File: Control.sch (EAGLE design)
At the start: 20 parts, among them IC1 MEGA8-P, Q1 16MHz, T1 2N2222, X1 MKDSN1,5/3-5,08, X2 MKDSN1,5/3-5,08

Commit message: updated schematic and board
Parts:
- added R7: 120K, rcl:R-US_0207/7
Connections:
- net GND: now also R7.2
- net N$18: now also R7.1
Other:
- moved on the sheet: PROG-HDR
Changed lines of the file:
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@@
 <part name="P+5" library="supply1" deviceset="+5V" device=""/>
 <part name="GND6" library="supply1" deviceset="GND" device=""/>
+<part name="R7" library="rcl" deviceset="R-US_" device="0207/7" value="120K"/>
+<part name="GND10" library="supply1" deviceset="GND" device=""/>
 </parts>
 <sheets>
@@
 <instance part="C2" gate="G$1" x="43.18" y="71.12"/>
 <instance part="IC1" gate="G$1" x="124.46" y="73.66"/>
-<instance part="PROG-HDR" gate="1" x="182.88" y="43.18"/>
+<instance part="PROG-HDR" gate="1" x="175.26" y="43.18"/>
 <instance part="P+1" gate="1" x="58.42" y="81.28"/>
 <instance part="P+2" gate="1" x="96.52" y="111.76"/>
@@
 <instance part="P+5" gate="1" x="86.36" y="66.04"/>
 <instance part="GND6" gate="1" x="86.36" y="53.34"/>
+<instance part="R7" gate="G$1" x="170.18" y="88.9" smashed="yes">
+<attribute name="NAME" x="166.37" y="90.3986" size="1.778" layer="95"/>
+<attribute name="VALUE" x="171.45" y="90.678" size="1.778" layer="96"/>
+</instance>
+<instance part="GND10" gate="1" x="175.26" y="86.36"/>
 </instances>
 <busses>
@@
 <pinref part="PROG-HDR" gate="1" pin="1"/>
 <pinref part="GND5" gate="1" pin="GND"/>
+<wire x1="182.88" y1="40.64" x2="190.5" y2="40.64" width="0.1524" layer="91"/>
 <wire x1="190.5" y1="40.64" x2="190.5" y2="38.1" width="0.1524" layer="91"/>
 </segment>
@@
 <pinref part="GND6" gate="1" pin="GND"/>
 </segment>
+<segment>
+<pinref part="R7" gate="G$1" pin="2"/>
+<pinref part="GND10" gate="1" pin="GND"/>
+</segment>
 </net>
 <net name="N$4" class="0">
@@
 <segment>
 <pinref part="IC1" gate="G$1" pin="PB4(MISO)"/>
-<wire x1="149.86" y1="45.72" x2="175.26" y2="45.72" width="0.1524" layer="91"/>
+<wire x1="149.86" y1="45.72" x2="167.64" y2="45.72" width="0.1524" layer="91"/>
 <pinref part="PROG-HDR" gate="1" pin="6"/>
 </segment>
@@
 <segment>
 <pinref part="IC1" gate="G$1" pin="PB5(SCK)"/>
-<wire x1="149.86" y1="43.18" x2="175.26" y2="43.18" width="0.1524" layer="91"/>
+<wire x1="149.86" y1="43.18" x2="167.64" y2="43.18" width="0.1524" layer="91"/>
 <pinref part="PROG-HDR" gate="1" pin="4"/>
 </segment>
@@
 <segment>
 <pinref part="PROG-HDR" gate="1" pin="2"/>
-<wire x1="175.26" y1="40.64" x2="175.26" y2="35.56" width="0.1524" layer="91"/>
-<wire x1="175.26" y1="35.56" x2="93.98" y2="35.56" width="0.1524" layer="91"/>
+<wire x1="167.64" y1="40.64" x2="167.64" y2="35.56" width="0.1524" layer="91"/>
+<wire x1="167.64" y1="35.56" x2="93.98" y2="35.56" width="0.1524" layer="91"/>
 <wire x1="93.98" y1="35.56" x2="93.98" y2="101.6" width="0.1524" layer="91"/>
 <pinref part="IC1" gate="G$1" pin="PC6(/RESET)"/>
@@
 <pinref part="PROG-HDR" gate="1" pin="5"/>
 <pinref part="P+3" gate="1" pin="+5V"/>
+<wire x1="182.88" y1="45.72" x2="190.5" y2="45.72" width="0.1524" layer="91"/>
 <wire x1="190.5" y1="45.72" x2="190.5" y2="50.8" width="0.1524" layer="91"/>
 </segment>
@@
 <wire x1="167.64" y1="55.88" x2="193.04" y2="55.88" width="0.1524" layer="91"/>
 <wire x1="193.04" y1="55.88" x2="193.04" y2="43.18" width="0.1524" layer="91"/>
-<wire x1="193.04" y1="43.18" x2="190.5" y2="43.18" width="0.1524" layer="91"/>
+<wire x1="193.04" y1="43.18" x2="182.88" y2="43.18" width="0.1524" layer="91"/>
 </segment>
 </net>
@@
 <pinref part="R1" gate="G$1" pin="1"/>
 <wire x1="149.86" y1="55.88" x2="165.1" y2="55.88" width="0.1524" layer="91"/>
-<wire x1="165.1" y1="55.88" x2="165.1" y2="96.52" width="0.1524" layer="91"/>
-</segment>
-</net>
+<wire x1="165.1" y1="55.88" x2="165.1" y2="88.9" width="0.1524" layer="91"/>
+<pinref part="R7" gate="G$1" pin="1"/>
+<wire x1="165.1" y1="88.9" x2="165.1" y2="96.52" width="0.1524" layer="91"/>
+<junction x="165.1" y="88.9"/>
+</segment>
+</net>

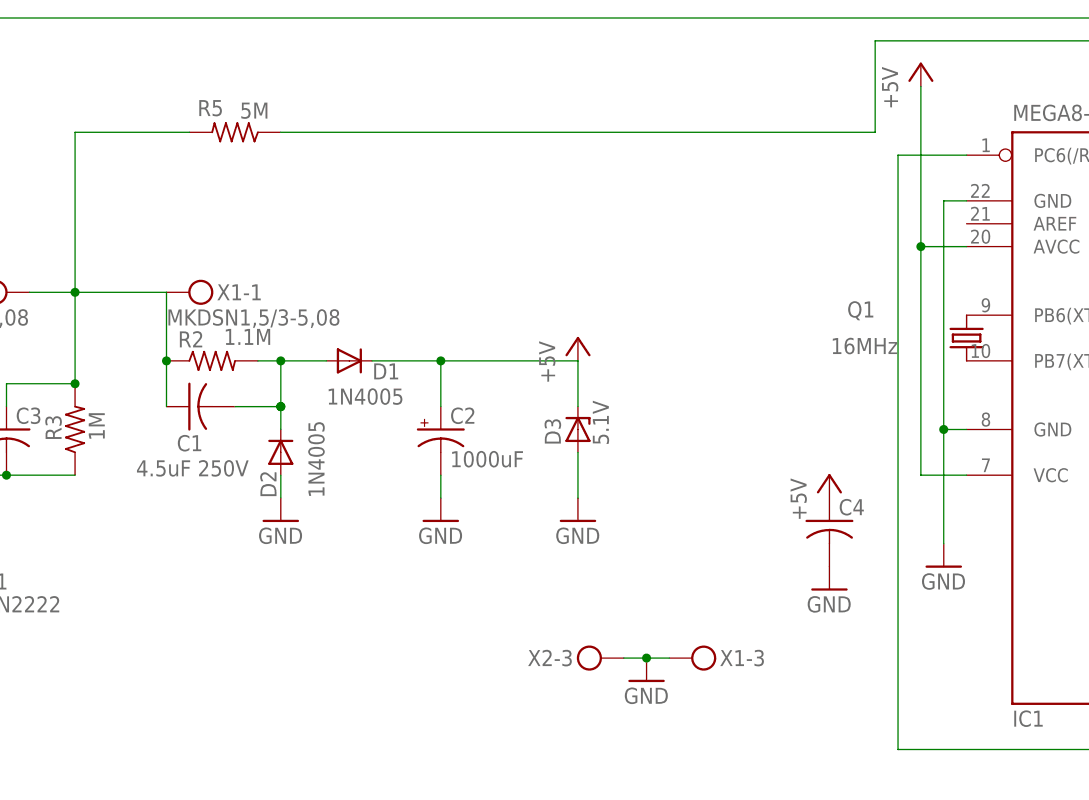
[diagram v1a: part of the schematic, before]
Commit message: Updated schematic and board to add needed pullup resistor to reset pin on Atmega. Also added surface mount pads for local filter capacitor. Pullup resistor located to fit inside central channel of a DIP socket. Changes needed discovered at first hardware assembly.
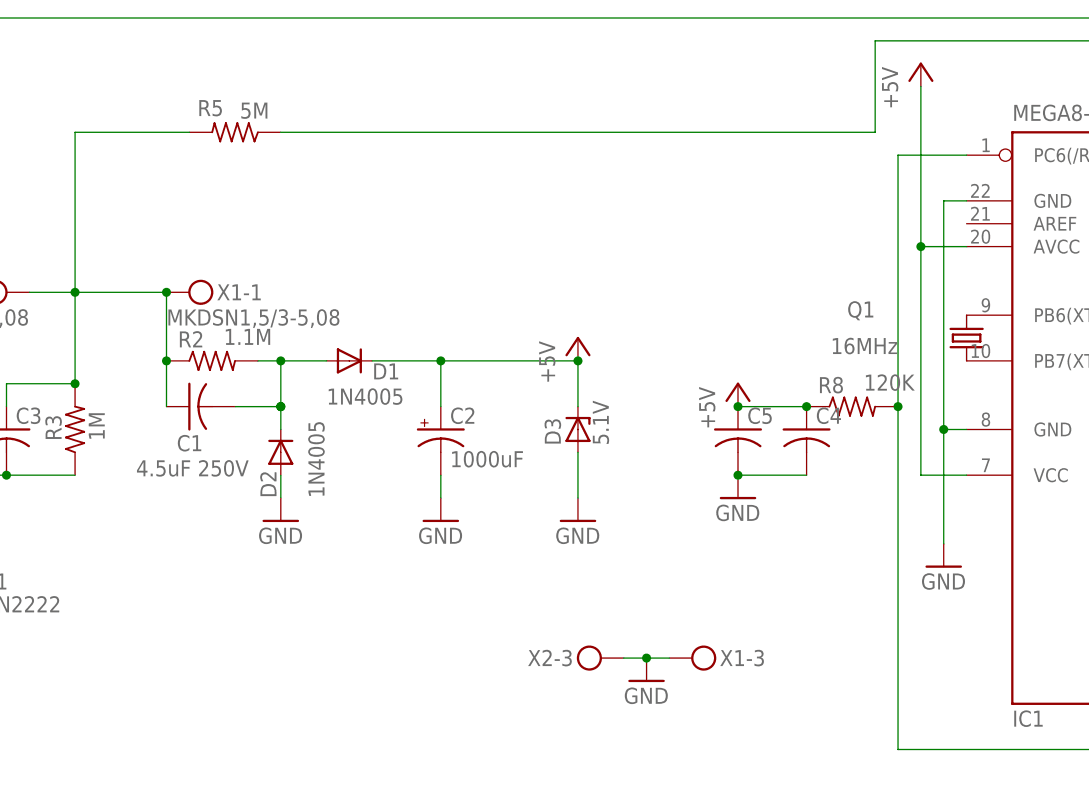
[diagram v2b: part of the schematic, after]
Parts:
- added C5: (no value), rcl:C-USC0402K
- added R8: 120K, rcl:R-US_0207/7
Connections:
- net +5V: now also C5.1, R8.1
- net GND: now also C5.2
- net N$8: now also R8.2
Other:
- moved on the sheet: C4
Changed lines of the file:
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@@
 <part name="R7" library="rcl" deviceset="R-US_" device="0207/7" value="120K"/>
 <part name="GND10" library="supply1" deviceset="GND" device=""/>
+<part name="R8" library="rcl" deviceset="R-US_" device="0207/7" value="120K"/>
+<part name="C5" library="rcl" deviceset="C-US" device="C0402K"/>
 </parts>
 <sheets>
@@
 <attribute name="VALUE" x="93.98" y="81.28" size="1.778" layer="96" rot="R180"/>
 </instance>
-<instance part="C4" gate="G$1" x="86.36" y="60.96"/>
-<instance part="P+5" gate="1" x="86.36" y="66.04"/>
-<instance part="GND6" gate="1" x="86.36" y="53.34"/>
+<instance part="C4" gate="G$1" x="83.82" y="71.12"/>
+<instance part="P+5" gate="1" x="76.2" y="76.2"/>
+<instance part="GND6" gate="1" x="76.2" y="63.5"/>
 <instance part="R7" gate="G$1" x="170.18" y="88.9" smashed="yes">
 <attribute name="NAME" x="166.37" y="90.3986" size="1.778" layer="95"/>
@@
 </instance>
 <instance part="GND10" gate="1" x="175.26" y="86.36"/>
+<instance part="R8" gate="G$1" x="88.9" y="73.66" smashed="yes">
+<attribute name="NAME" x="85.09" y="75.1586" size="1.778" layer="95"/>
+<attribute name="VALUE" x="90.17" y="75.438" size="1.778" layer="96"/>
+</instance>
+<instance part="C5" gate="G$1" x="76.2" y="71.12"/>
 </instances>
 <busses>
@@
 <pinref part="C4" gate="G$1" pin="2"/>
 <pinref part="GND6" gate="1" pin="GND"/>
+<wire x1="76.2" y1="66.04" x2="83.82" y2="66.04" width="0.1524" layer="91"/>
+<pinref part="C5" gate="G$1" pin="2"/>
+<junction x="76.2" y="66.04"/>
 </segment>
 <segment>
@@
 <wire x1="167.64" y1="40.64" x2="167.64" y2="35.56" width="0.1524" layer="91"/>
 <wire x1="167.64" y1="35.56" x2="93.98" y2="35.56" width="0.1524" layer="91"/>
-<wire x1="93.98" y1="35.56" x2="93.98" y2="101.6" width="0.1524" layer="91"/>
+<wire x1="93.98" y1="35.56" x2="93.98" y2="73.66" width="0.1524" layer="91"/>
 <pinref part="IC1" gate="G$1" pin="PC6(/RESET)"/>
+<wire x1="93.98" y1="73.66" x2="93.98" y2="101.6" width="0.1524" layer="91"/>
 <wire x1="93.98" y1="101.6" x2="101.6" y2="101.6" width="0.1524" layer="91"/>
+<pinref part="R8" gate="G$1" pin="2"/>
+<junction x="93.98" y="73.66"/>
 </segment>
 </net>
@@
 <wire x1="58.42" y1="78.74" x2="43.18" y2="78.74" width="0.1524" layer="91"/>
 <junction x="43.18" y="78.74"/>
+<junction x="58.42" y="78.74"/>
 </segment>
 <segment>
@@
 <pinref part="C4" gate="G$1" pin="1"/>
 <pinref part="P+5" gate="1" pin="+5V"/>
+<pinref part="R8" gate="G$1" pin="1"/>
+<wire x1="76.2" y1="73.66" x2="83.82" y2="73.66" width="0.1524" layer="91"/>
+<junction x="83.82" y="73.66"/>
+<pinref part="C5" gate="G$1" pin="1"/>
+<junction x="76.2" y="73.66"/>
 </segment>
 </net>
@@
 <junction x="2.54" y="86.36"/>
 <junction x="2.54" y="76.2"/>
+<junction x="12.7" y="86.36"/>
 </segment>
 </net>
@@
 </sheet>
 </sheets>
+<errors>
+</errors>
 </schematic>
 </drawing>

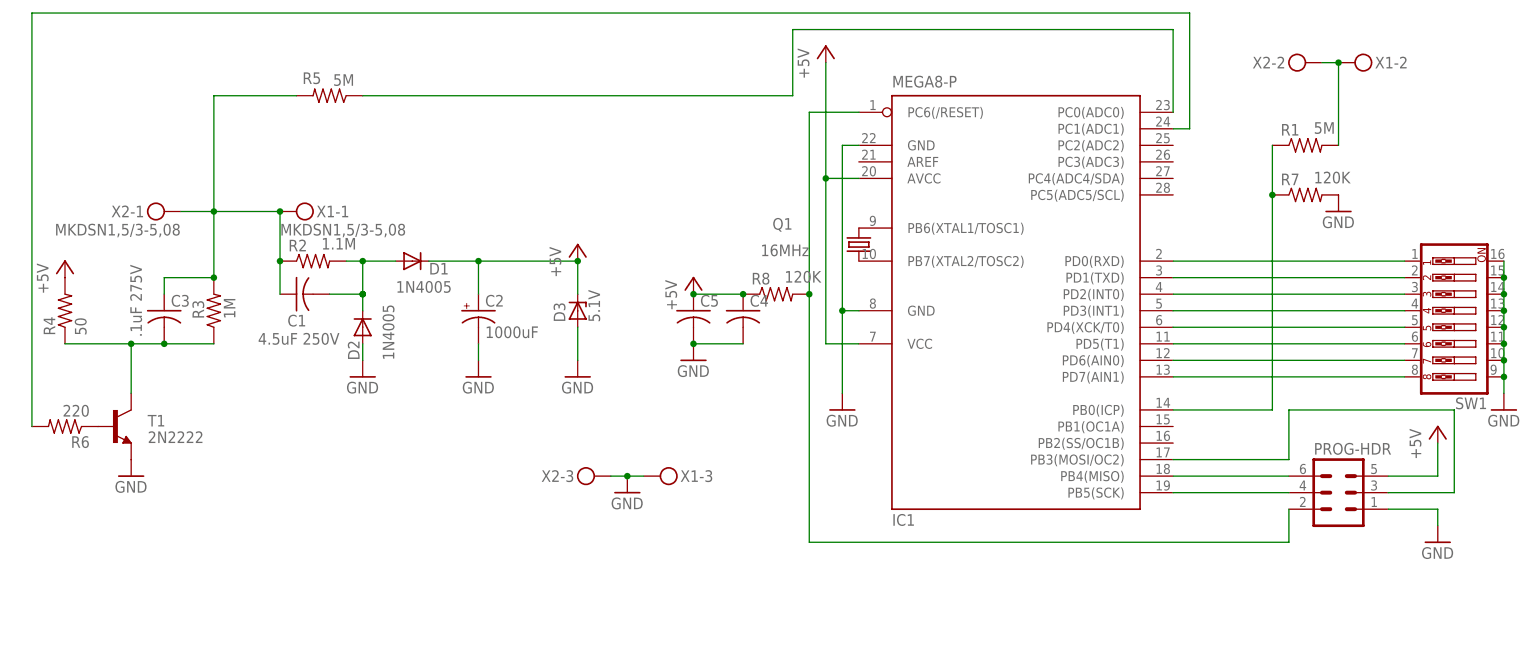
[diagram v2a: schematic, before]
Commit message: Added surface mount options for low voltage section
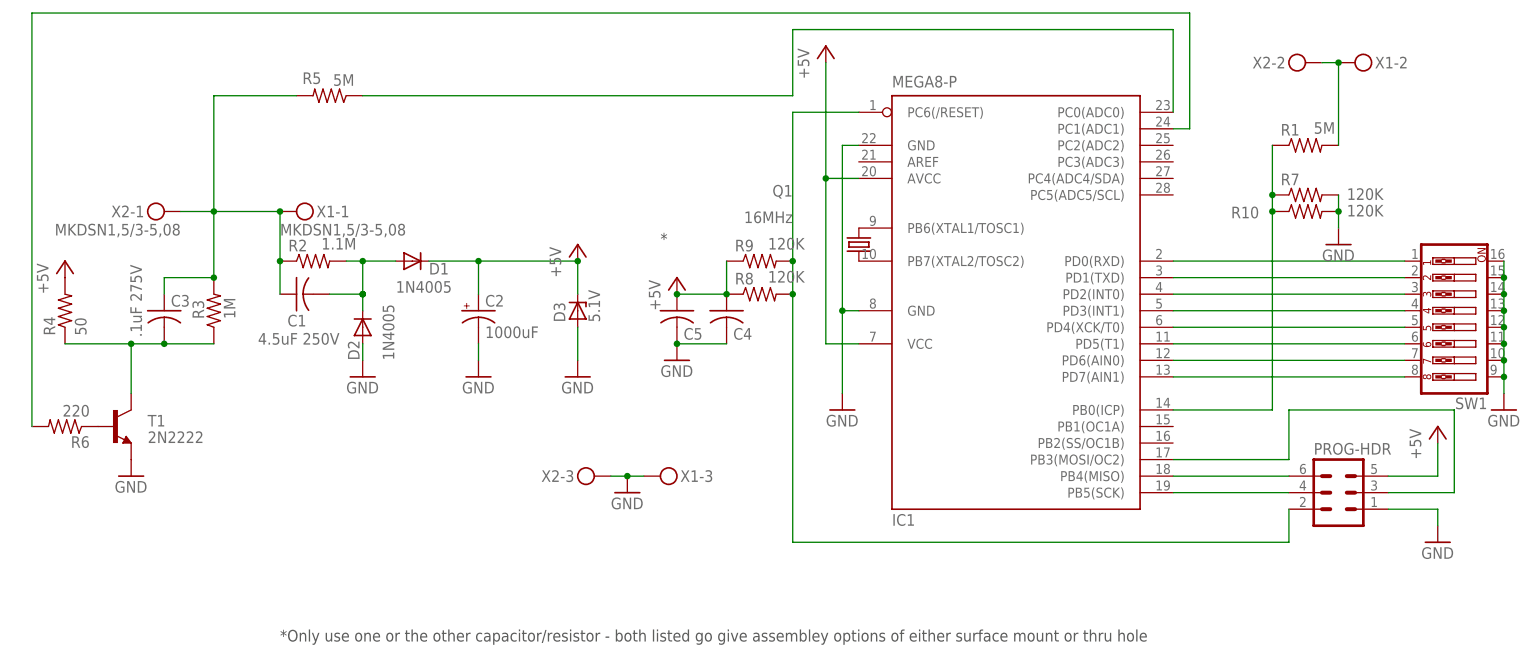
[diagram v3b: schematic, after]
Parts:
- added R10, R9: 120K, rcl:R-US_M0805
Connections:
- net +5V: now also R9.1
- net GND: now also R10.2
- net N$18: now also R10.1
- net N$8: now also R9.2
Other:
- note added: "*"
- note added: "*Only use one or the other capacitor/resistor - both listed go give assembley options of either surface mount or thru hole"
- moved on the sheet: C4, C5, R8
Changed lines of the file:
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@@
 <part name="R8" library="rcl" deviceset="R-US_" device="0207/7" value="120K"/>
 <part name="C5" library="rcl" deviceset="C-US" device="C0402K"/>
+<part name="R9" library="rcl" deviceset="R-US_" device="M0805" value="120K"/>
+<part name="R10" library="rcl" deviceset="R-US_" device="M0805" value="120K"/>
 </parts>
 <sheets>
 <sheet>
 <plain>
+<text x="12.7" y="20.32" size="1.778" layer="97">*Only use one or the other capacitor/resistor - both listed go give assembley options of either surface mount or thru hole</text>
+<text x="71.12" y="81.28" size="1.778" layer="97">*</text>
+<polygon width="0.1524" layer="98">
+<vertex x="73.66" y="83.82"/>
+<vertex x="93.98" y="83.82"/>
+<vertex x="93.98" y="55.88"/>
+<vertex x="68.58" y="55.88"/>
+<vertex x="68.58" y="83.82"/>
+</polygon>
 </plain>
 <instances>
@@
 <instance part="GND9" gate="1" x="200.66" y="55.88"/>
 <instance part="Q1" gate="G$1" x="101.6" y="81.28" smashed="yes" rot="R90">
-<attribute name="NAME" x="91.44" y="85.344" size="1.778" layer="95" rot="R180"/>
-<attribute name="VALUE" x="93.98" y="81.28" size="1.778" layer="96" rot="R180"/>
-</instance>
-<instance part="C4" gate="G$1" x="83.82" y="71.12"/>
-<instance part="P+5" gate="1" x="76.2" y="76.2"/>
-<instance part="GND6" gate="1" x="76.2" y="63.5"/>
+<attribute name="NAME" x="91.44" y="90.424" size="1.778" layer="95" rot="R180"/>
+<attribute name="VALUE" x="91.44" y="86.36" size="1.778" layer="96" rot="R180"/>
+</instance>
+<instance part="C4" gate="G$1" x="81.28" y="71.12" smashed="yes">
+<attribute name="NAME" x="82.296" y="66.675" size="1.778" layer="95"/>
+<attribute name="VALUE" x="82.296" y="66.929" size="1.778" layer="96"/>
+</instance>
+<instance part="P+5" gate="1" x="73.66" y="76.2"/>
+<instance part="GND6" gate="1" x="73.66" y="63.5"/>
 <instance part="R7" gate="G$1" x="170.18" y="88.9" smashed="yes">
 <attribute name="NAME" x="166.37" y="90.3986" size="1.778" layer="95"/>
-<attribute name="VALUE" x="171.45" y="90.678" size="1.778" layer="96"/>
-</instance>
-<instance part="GND10" gate="1" x="175.26" y="86.36"/>
-<instance part="R8" gate="G$1" x="88.9" y="73.66" smashed="yes">
-<attribute name="NAME" x="85.09" y="75.1586" size="1.778" layer="95"/>
-<attribute name="VALUE" x="90.17" y="75.438" size="1.778" layer="96"/>
-</instance>
-<instance part="C5" gate="G$1" x="76.2" y="71.12"/>
+<attribute name="VALUE" x="176.53" y="88.138" size="1.778" layer="96"/>
+</instance>
+<instance part="GND10" gate="1" x="175.26" y="81.28"/>
+<instance part="R8" gate="G$1" x="86.36" y="73.66" smashed="yes">
+<attribute name="NAME" x="82.55" y="75.1586" size="1.778" layer="95"/>
+<attribute name="VALUE" x="87.63" y="75.438" size="1.778" layer="96"/>
+</instance>
+<instance part="C5" gate="G$1" x="73.66" y="71.12" smashed="yes">
+<attribute name="NAME" x="74.676" y="66.675" size="1.778" layer="95"/>
+<attribute name="VALUE" x="74.676" y="66.929" size="1.778" layer="96"/>
+</instance>
+<instance part="R9" gate="G$1" x="86.36" y="78.74" smashed="yes">
+<attribute name="NAME" x="82.55" y="80.2386" size="1.778" layer="95"/>
+<attribute name="VALUE" x="87.63" y="80.518" size="1.778" layer="96"/>
+</instance>
+<instance part="R10" gate="G$1" x="170.18" y="86.36" smashed="yes">
+<attribute name="NAME" x="158.75" y="85.3186" size="1.778" layer="95"/>
+<attribute name="VALUE" x="176.53" y="85.598" size="1.778" layer="96"/>
+</instance>
 </instances>
 <busses>
@@
 <pinref part="C4" gate="G$1" pin="2"/>
 <pinref part="GND6" gate="1" pin="GND"/>
-<wire x1="76.2" y1="66.04" x2="83.82" y2="66.04" width="0.1524" layer="91"/>
+<wire x1="73.66" y1="66.04" x2="81.28" y2="66.04" width="0.1524" layer="91"/>
 <pinref part="C5" gate="G$1" pin="2"/>
-<junction x="76.2" y="66.04"/>
+<junction x="73.66" y="66.04"/>
 </segment>
 <segment>
 <pinref part="R7" gate="G$1" pin="2"/>
 <pinref part="GND10" gate="1" pin="GND"/>
+<wire x1="175.26" y1="83.82" x2="175.26" y2="86.36" width="0.1524" layer="91"/>
+<pinref part="R10" gate="G$1" pin="2"/>
+<wire x1="175.26" y1="86.36" x2="175.26" y2="88.9" width="0.1524" layer="91"/>
+<junction x="175.26" y="86.36"/>
 </segment>
 </net>
@@
 <pinref part="PROG-HDR" gate="1" pin="2"/>
 <wire x1="167.64" y1="40.64" x2="167.64" y2="35.56" width="0.1524" layer="91"/>
-<wire x1="167.64" y1="35.56" x2="93.98" y2="35.56" width="0.1524" layer="91"/>
-<wire x1="93.98" y1="35.56" x2="93.98" y2="73.66" width="0.1524" layer="91"/>
+<wire x1="167.64" y1="35.56" x2="91.44" y2="35.56" width="0.1524" layer="91"/>
+<wire x1="91.44" y1="35.56" x2="91.44" y2="73.66" width="0.1524" layer="91"/>
 <pinref part="IC1" gate="G$1" pin="PC6(/RESET)"/>
-<wire x1="93.98" y1="73.66" x2="93.98" y2="101.6" width="0.1524" layer="91"/>
-<wire x1="93.98" y1="101.6" x2="101.6" y2="101.6" width="0.1524" layer="91"/>
+<wire x1="91.44" y1="73.66" x2="91.44" y2="78.74" width="0.1524" layer="91"/>
+<wire x1="91.44" y1="78.74" x2="91.44" y2="101.6" width="0.1524" layer="91"/>
+<wire x1="91.44" y1="101.6" x2="101.6" y2="101.6" width="0.1524" layer="91"/>
 <pinref part="R8" gate="G$1" pin="2"/>
-<junction x="93.98" y="73.66"/>
+<junction x="91.44" y="73.66"/>
+<pinref part="R9" gate="G$1" pin="2"/>
+<junction x="91.44" y="78.74"/>
 </segment>
 </net>
@@
 <pinref part="P+5" gate="1" pin="+5V"/>
 <pinref part="R8" gate="G$1" pin="1"/>
-<wire x1="76.2" y1="73.66" x2="83.82" y2="73.66" width="0.1524" layer="91"/>
-<junction x="83.82" y="73.66"/>
+<wire x1="73.66" y1="73.66" x2="81.28" y2="73.66" width="0.1524" layer="91"/>
+<junction x="81.28" y="73.66"/>
 <pinref part="C5" gate="G$1" pin="1"/>
-<junction x="76.2" y="73.66"/>
+<junction x="73.66" y="73.66"/>
+<pinref part="R9" gate="G$1" pin="1"/>
+<wire x1="81.28" y1="73.66" x2="81.28" y2="78.74" width="0.1524" layer="91"/>
 </segment>
 </net>
@@
 <pinref part="R1" gate="G$1" pin="1"/>
 <wire x1="149.86" y1="55.88" x2="165.1" y2="55.88" width="0.1524" layer="91"/>
-<wire x1="165.1" y1="55.88" x2="165.1" y2="88.9" width="0.1524" layer="91"/>
+<wire x1="165.1" y1="55.88" x2="165.1" y2="86.36" width="0.1524" layer="91"/>
 <pinref part="R7" gate="G$1" pin="1"/>
+<wire x1="165.1" y1="86.36" x2="165.1" y2="88.9" width="0.1524" layer="91"/>
 <wire x1="165.1" y1="88.9" x2="165.1" y2="96.52" width="0.1524" layer="91"/>
 <junction x="165.1" y="88.9"/>
-</segment>
-</net>
+<pinref part="R10" gate="G$1" pin="1"/>
+<junction x="165.1" y="86.36"/>
+</segment>
+</net>

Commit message: Slight board size reduction
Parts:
- D3: device diode:ZENER-DIODEP1-Z12 -> diode:ZENER-DIODEDO34-7
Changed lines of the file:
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@@
 <part name="P+2" library="supply1" deviceset="+5V" device=""/>
 <part name="P+3" library="supply1" deviceset="+5V" device=""/>
-<part name="D3" library="diode" deviceset="ZENER-DIODE" device="P1-Z12" value="5.1V"/>
+<part name="D3" library="diode" deviceset="ZENER-DIODE" device="DO34-7" value="5.1V"/>
 <part name="GND7" library="supply1" deviceset="GND" device=""/>
 <part name="SW1" library="special" deviceset="SW_DIP-8" device=""/>
